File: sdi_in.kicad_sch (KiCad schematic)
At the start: 18 parts, among them U3 LMH0344SQE_NOPB

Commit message: implement schematic review feedback
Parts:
- added C73, C77: 100n, Capacitor_SMD:C_0603_1608Metric, symbol Device:C
- C5: renamed from C12; value 100n -> 1u; footprint Capacitor_SMD:C_0402_1005Metric -> Capacitor_SMD:C_0603_1608Metric
- C6: renamed from C10; footprint Capacitor_SMD:C_0402_1005Metric -> Capacitor_SMD:C_0603_1608Metric
- C7: renamed from C11; footprint Capacitor_SMD:C_0402_1005Metric -> Capacitor_SMD:C_0603_1608Metric
- renumbered C1 to C2, C14 to C3, C15 to C4, C2 to C8, D2 to D1, R4 to R3, R6 to R4, R3 to R6, R46 to R7, R50 to R8, R54 to R9, U3 to U1
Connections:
- net +3V3: now also C73.1, C77.1
- net GND: now also C73.2, C77.2; no longer R8.2
- new net ~{VIO_GOOD}: R8.2
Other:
- moved on the sheet: R8, R9

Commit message: substitute bnc connector for better max freq
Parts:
- removed RF1: DOSIN-801-0057, JLCImport:DOSIN-801-0057, symbol JLCImport:DOSIN-801-0057
- added J1: Conn_Coaxial, JLCImport:CONN_73171-1900_MOL, symbol Connector:Conn_Coaxial
- renumbered C77 to C10, C73 to C9, R8 to R10, R9 to R11, R3 to R5, R4 to R6, R5 to R7, R6 to R8, R7 to R9
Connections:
- net GND: now also J1.2 (Ext)
- net at C2.1, L1.1, R5.1: now also J1.1 (In)

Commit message: split gpio expanders by inputs/outputs instead of quads
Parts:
- C10, C2, C3, C4, C5, C6, C7, C8, C9, D1, L1, R10, R11, R5, R6, R7, R8, R9: KiLib_Generator (none) -> SMD_2terminal_chip_molded
- U1: KiLib_Generator (none) -> package/no_lead

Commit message: finish layout of first in and out channel
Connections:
- net SDO+: now reaches C6.1, U1.11 (SDO)
- net SDO-: now reaches C7.1, U1.10 (SDO#)
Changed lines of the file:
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@@
+		)
+	)
+	(label "SDO+"
+		(at 142.1905 74.93 0)
+		(effects
+			(font
+				(size 1.27 1.27)
+			)
+			(justify left bottom)
+		)
+	)
+	(label "SDO-"
+		(at 142.1905 77.47 0)
+		(effects
+			(font
+				(size 1.27 1.27)
+			)
+			(justify left bottom)
 		)
 	)
@@
 		(polyline
 			(pts
-				(xy 89.535 66.04) (xy 89.535 76.2) (xy 88.265 76.2) (xy 88.265 66.04)
+				(xy 99.695 66.04) (xy 99.695 70.485) (xy 100.965 70.485) (xy 100.965 66.04)
+			)
+			(stroke
+				(width 0)
+				(type dash)
+			)
+			(fill
+				(type none)
+			)
+		)
+	)
+	(rule_area
+		(exclude_from_sim no)
+		(in_bom yes)
+		(on_board yes)
+		(dnp no)
+		(polyline
+			(pts
+				(xy 80.645 66.04) (xy 80.645 70.485) (xy 81.915 70.485) (xy 81.915 66.04)
 			)
 			(stroke
@@
 			(pts
 				(xy 149.225 68.58) (xy 149.225 78.74) (xy 150.495 78.74) (xy 150.495 68.58)
-			)
-			(stroke
-				(width 0)
-				(type dash)
-			)
-			(fill
-				(type none)
-			)
-		)
-	)
-	(rule_area
-		(exclude_from_sim no)
-		(in_bom yes)
-		(on_board yes)
-		(dnp no)
-		(polyline
-			(pts
-				(xy 99.695 66.04) (xy 99.695 76.2) (xy 100.965 76.2) (xy 100.965 66.04)
 			)
 			(stroke
@@
 			(justify left bottom)
 		)
-		(property "Netclass" "75 Ohm Diff"
+		(property "Netclass" "75 Ohm Single"
 			(at 97.536 61.468 0)
 			(show_name no)
@@
 		(length 2.54)
 		(shape round)
-		(at 88.9 66.04 0)
-		(effects
-			(font
-				(size 1.27 1.27)
-			)
-			(justify left bottom)
-		)
-		(property "Netclass" "75 Ohm Diff"
-			(at 91.694 61.468 0)
-			(show_name no)
-			(do_not_autoplace no)
-			(effects
-				(font
-					(size 1.27 1.27)
-				)
-				(justify right)
+		(at 81.28 66.04 0)
+		(effects
+			(font
+				(size 1.27 1.27)
+			)
+			(justify left bottom)
+		)
+		(property "Netclass" "75 Ohm Single"
+			(at 78.486 61.468 0)
+			(show_name no)
+			(do_not_autoplace no)
+			(effects
+				(font
+					(size 1.27 1.27)
+				)
+				(justify left)
 			)
 		)
 		(property "Component Class" ""
-			(at 274.32 1.27 0)
-			(show_name no)
-			(do_not_autoplace no)
+			(at -104.14 1.27 0)
+			(show_name no)
+			(do_not_autoplace no)

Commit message: route all in/out lanes
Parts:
- U1: footprint Package_DFN_QFN:Texas_RUM0016A_WQFN-16-1EP_4x4mm_P0.65mm_EP2.6x2.6mm_ThermalVias -> JLCImport:WQFN-16-1EP_4x4mm_P0.65mm_EP2.6x2.6mm_ThermalVias
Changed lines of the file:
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@@
 			)
 		)
-		(property "Footprint" "Package_DFN_QFN:Texas_RUM0016A_WQFN-16-1EP_4x4mm_P0.65mm_EP2.6x2.6mm_ThermalVias"
+		(property "Footprint" "JLCImport:WQFN-16-1EP_4x4mm_P0.65mm_EP2.6x2.6mm_ThermalVias"
 			(at 127 77.47 0)
 			(hide yes)

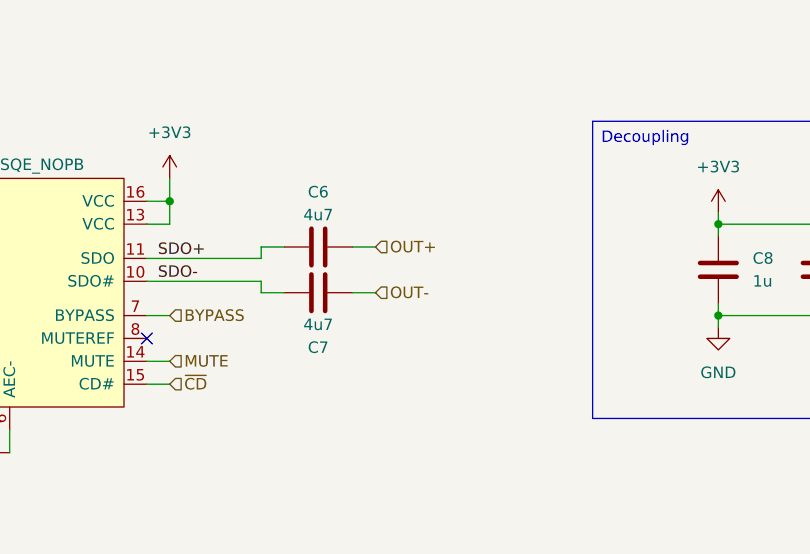
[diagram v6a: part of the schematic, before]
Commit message: route the smartvio mcu and the gpio expanders
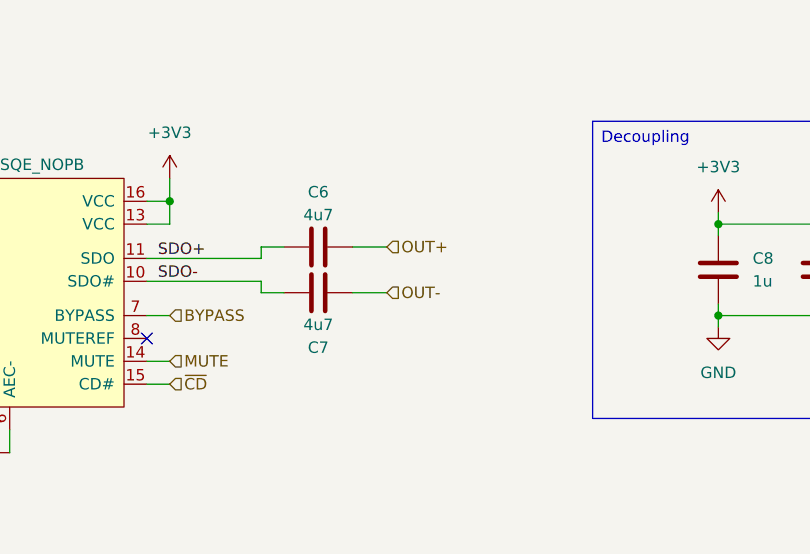
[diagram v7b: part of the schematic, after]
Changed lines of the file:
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@@
 	(wire
 		(pts
-			(xy 166.37 73.66) (xy 163.83 73.66)
+			(xy 167.64 73.66) (xy 163.83 73.66)
 		)
 		(stroke
@@
 	(wire
 		(pts
-			(xy 166.37 78.74) (xy 163.83 78.74)
+			(xy 167.64 78.74) (xy 163.83 78.74)
 		)
 		(stroke
@@
 	(hierarchical_label "OUT+"
 		(shape input)
-		(at 166.37 73.66 0)
+		(at 167.64 73.66 0)
 		(effects
 			(font
@@
 	(hierarchical_label "OUT-"
 		(shape input)
-		(at 166.37 78.74 0)
+		(at 167.64 78.74 0)
 		(effects
 			(font
@@
 			(pts
 				(xy 99.695 66.04) (xy 99.695 70.485) (xy 100.965 70.485) (xy 100.965 66.04)
+			)
+			(stroke
+				(width 0)
+				(type dash)
+			)
+			(fill
+				(type none)
+			)
+		)
+	)
+	(rule_area
+		(exclude_from_sim no)
+		(in_bom yes)
+		(on_board yes)
+		(dnp no)
+		(polyline
+			(pts
+				(xy 164.465 71.12) (xy 164.465 81.28) (xy 165.735 81.28) (xy 165.735 71.12)
 			)
 			(stroke
@@
 			(show_name no)
 			(do_not_autoplace no)
+			(effects
+				(font
+					(size 1.27 1.27)
+					(italic yes)
+				)
+			)
+		)
+	)
+	(netclass_flag ""
+		(length 2.54)
+		(shape round)
+		(at 165.1 71.12 0)
+		(effects
+			(font
+				(size 1.27 1.27)
+			)
+			(justify left bottom)
+		)
+		(property "Netclass" "100 Ohm Diff"
+			(at 162.306 66.548 0)
+			(show_name no)
+			(do_not_autoplace no)
+			(effects
+				(font
+					(size 1.27 1.27)
+				)
+				(justify left)
+			)
+		)
+		(property "Component Class" ""
+			(at -20.32 6.35 0)
+			(show_name no)
+			(do_not_autoplace no)

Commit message: finish routing
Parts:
- J1: Manufacturer (none) -> Molex; Manufacturer Part (none) -> 731711900
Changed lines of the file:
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@@
 			)
 		)
-		(property "Datasheet" ""
+		(property "Datasheet" "https://www.molex.com/en-us/products/part-detail/731711900?display=pdf"
 			(at 54.61 68.58 0)
 			(hide yes)
@@
 			(at 54.61 68.58 0)
 			(hide yes)
+			(show_name no)
+			(do_not_autoplace no)
+			(effects
+				(font
+					(size 1.27 1.27)
+				)
+			)
+		)
+		(property "Manufacturer" "Molex"
+			(at 54.61 68.58 0)
+			(hide yes)
+			(show_name no)
+			(do_not_autoplace no)
+			(effects
+				(font
+					(size 1.27 1.27)
+				)
+			)
+		)
+		(property "Manufacturer Part" "731711900"
+			(at 54.61 68.58 0)
+			(hide yes)
